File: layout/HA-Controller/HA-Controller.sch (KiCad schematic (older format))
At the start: 62 parts, among them J1 Conn_01x03, J2 Conn_01x06, J3 Conn_01x08, J4 Conn_01x10, J5 Conn_01x08, J6 Conn_01x15, J7 Conn_01x15, J8 Conn_01x04, J9 Conn_01x04, K1 FINDER-44.62, K2 FINDER-44.62, M1 Jumper, M2 Jumper, Q1 BC547, Q2 BC547, U1 ESP-12E, U2 IRM-15-24, U3 TSR_1-2450

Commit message: Layout abgespeckt
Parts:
- removed 180K: 1K2, Resistor_THT:R_Axial_DIN0309_L9.0mm_D3.2mm_P12.70mm_Horizontal, symbol Device:R
- removed C4, C6, C8: 100n, Capacitor_SMD:C_0603_1608Metric, symbol Device:C_Small
- removed C7: 10uF/50V, Capacitor_THT:CP_Radial_D6.3mm_P2.50mm, symbol Device:CP_Small
- removed D1: 1N4148, Diode_THT:D_DO-35_SOD27_P7.62mm_Horizontal, symbol Diode:1N4148
- removed D3, D6: LED_Small, LED_THT:LED_D3.0mm, symbol Device:LED_Small
- removed F1: 0,1A, Fuse:Fuseholder_Cylinder-5x20mm_Stelvio-Kontek_PTF78_Horizontal_Open, symbol Device:Fuse_Small
- removed J1: Conn_01x03, Connector_Phoenix_MSTB:PhoenixContact_MSTBA_2,5_3-G-5,08_1x03_P5.08mm_Horizontal, symbol Connector_Generic:Conn_01x03
- removed J3, J5: Conn_01x08, Connector_PinSocket_2.54mm:PinSocket_1x08_P2.54mm_Vertical, symbol Connector_Generic:Conn_01x08
- removed JP1: Jumper_NC_Small, Connector_PinHeader_2.54mm:PinHeader_1x02_P2.54mm_Vertical, symbol Device:Jumper_NC_Small
- removed K2: FINDER-44.62, Relay_THT:Relay_DPDT_Finder_40.52, symbol Relay:FINDER-44.62
- removed M1: Jumper, kp-Bom_only:Jumper, symbol kp-Bom_only:Jumper
- removed Q1: BC547, Package_TO_SOT_THT:TO-92_Inline, symbol Transistor_BJT:BC547
- removed R1: 4K7, Resistor_THT:R_Axial_DIN0309_L9.0mm_D3.2mm_P12.70mm_Horizontal, symbol Device:R
- removed R15, R9: 1K5, Resistor_THT:R_Axial_DIN0309_L9.0mm_D3.2mm_P12.70mm_Horizontal, symbol Device:R
- removed R2: 470, Resistor_THT:R_Axial_DIN0309_L9.0mm_D3.2mm_P12.70mm_Horizontal, symbol Device:R
- removed R5: dnf_470, Resistor_THT:R_Axial_DIN0309_L9.0mm_D3.2mm_P12.70mm_Horizontal, symbol Device:R
- removed R6: dnf_2K2, Resistor_THT:R_Axial_DIN0309_L9.0mm_D3.2mm_P12.70mm_Horizontal, symbol Device:R
- removed RV2: 24V, Varistor:RV_Disc_D7mm_W3.4mm_P5mm, symbol Device:Varistor
- removed U1: ESP-12E, RF_Module:ESP-12E, symbol RF_Module:ESP-12E
- removed U2: IRM-15-24, Zielke:NT-Meanwell-IRM-15, symbol Powersupply:Powersupply
- removed U3: TSR_1-2450, Converter_DCDC:Converter_DCDC_TRACO_TSR-1_THT, symbol Regulator_Switching:TSR_1-2450
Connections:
- net +24V is gone; now on net +5V: D2.1 (K), J4.5 (Pin_5), K1.A1, R10.1
- net K2-12 is gone; now on net +5V: J2.1 (Pin_1)
- net K2-14 is gone; now on net GND: J2.2 (Pin_2)
- net SWMaxNC is gone; now on net GPIO12: J4.4 (Pin_4), RV1.1
- net ADC: no longer names the net of J6.1 (Pin_1)
- net K2-11: no longer names the net of J2.3 (Pin_3)
- net Level: no longer names the net of J4.2 (Pin_2)
- net SWPumpOff renamed SW_Reserved
- no-connect marks 12 -> 11
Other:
- note added: "Door = close = 0V"
- note added: "GND"
- note added: "Open Door"
- note added: "S2\nclosed=\nReserved on\nopen =\nReserved off"
- note added: "SWDoor"
- note added: "SW_Reserved"
- note removed: "(0-1,054V)"
- note removed: "(10K)"
- note removed: "(2K2)"
- note removed: "(470)"
- note removed: "0-3.235V"
- note removed: "0-5V"
- note removed: "230V"
- note removed: "L1"
- note removed: "Max = close = 0V"
- note removed: "N"
- note removed: "Pump L1"
- note removed: "Pump N"
- note removed: "S1 (On/Off)"
- note removed: "S2 (Auto/Off)\nclosed=\nPump on\nopen =\nPump off"
- note removed: "S2\nclosed=\nPump on\nopen =\nPump off"
- note removed: "SWMaxNC"
- note removed: "SWPumpOff"

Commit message: Layout abgespeckt
Signed-off-by: Claus Zielke <info@cszielke.de>
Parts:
- removed J4: Conn_01x10, Connector_Phoenix_MSTB:PhoenixContact_MSTBA_2,5_10-G-5,08_1x10_P5.08mm_Horizontal, symbol Connector_Generic:Conn_01x10
- removed K1: FINDER-44.62, Relay_THT:Relay_DPDT_Finder_40.52, symbol Relay:FINDER-44.62
- removed R13: 1K, Resistor_THT:R_Axial_DIN0309_L9.0mm_D3.2mm_P12.70mm_Horizontal, symbol Device:R
- removed RV1, RV3, RV4: 24V, Varistor:RV_Disc_D7mm_W3.4mm_P5mm, symbol Device:Varistor
- added J4: Conn_01x06, Connector_Phoenix_MSTB:PhoenixContact_MSTBA_2,5_6-G-5,08_1x06_P5.08mm_Horizontal, symbol Connector_Generic:Conn_01x06
- added K1: G5V-2, Relay_THT:Relay_DPDT_Omron_G5V-2, symbol Relay:G5V-2
- R11: value 47K -> 3K3
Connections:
- net +5V: now also J4.4 (Pin_4), K1.1
- net GND: now also R12.2, J4.1 (Pin_1)
- net GPIO12: now also J4.2 (Pin_2)
- net K1-11: now also K1.13, K1.4
- net K1-12: now also K1.11, K1.6
- net K1-14: now also K1.8, K1.9
- net SW_Reserved: now also J4.3 (Pin_3)
- net at D2.2 (A), D4.1 (K), Q2.1 (C): now also K1.16
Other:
- note added: "2.9V"
- note removed: "0-29V"
- note removed: "0-3,13V"
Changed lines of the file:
@@
 $EndComp
 $Comp
-L Connector_Generic:Conn_01x10 J4
-U 1 1 5F26FC1D
-P 10050 3750
-F 0 "J4" H 10000 4350 50  0000 L CNN
-F 1 "Conn_01x10" H 10000 4250 50  0000 L CNN
-F 2 "Connector_Phoenix_MSTB:PhoenixContact_MSTBA_2,5_10-G-5,08_1x10_P5.08mm_Horizontal" H 10050 3750 50  0001 C CNN
-F 3 "~" H 10050 3750 50  0001 C CNN
-	1    10050 3750
-	1    0    0    -1
-$EndComp
-$Comp
 L Connector_Generic:Conn_01x06 J2
 U 1 1 5F272DC4
@@
 Wire Wire Line
 	9800 2650 9400 2650
-Wire Wire Line
-	9450 3950 9850 3950
-Wire Wire Line
-	9500 4250 9850 4250
-Text Label 9500 3350 0    50   ~ 0
+Text Label 9500 3550 0    50   ~ 0
 GND
 $Comp
 L power:GND #PWR02
 U 1 1 5F2781D4
-P 8350 3350
-F 0 "#PWR02" H 8350 3100 50  0001 C CNN
-F 1 "GND" H 8355 3177 50  0000 C CNN
-F 2 "" H 8350 3350 50  0001 C CNN
-F 3 "" H 8350 3350 50  0001 C CNN
-	1    8350 3350
-	0    1    1    0
+P 9400 3550
+F 0 "#PWR02" H 9400 3300 50  0001 C CNN
+F 1 "GND" H 9405 3377 50  0000 C CNN
+F 2 "" H 9400 3550 50  0001 C CNN
+F 3 "" H 9400 3550 50  0001 C CNN
+	1    9400 3550
+	-1   0    0    1
 $EndComp
-Wire Wire Line
-	8350 3350 8650 3350
 Text Label 9500 3650 0    50   ~ 0
 GPIO12
@@
 	7250 2150 7250 2100
 Connection ~ 7250 2150
-$Comp
-L Device:Varistor RV1
-U 1 1 5F3952B4
-P 8650 3150
-F 0 "RV1" H 8753 3196 50  0000 L CNN
-F 1 "24V" H 8753 3105 50  0000 L CNN
-F 2 "Varistor:RV_Disc_D7mm_W3.4mm_P5mm" V 8580 3150 50  0001 C CNN
-F 3 "~" H 8650 3150 50  0001 C CNN
-	1    8650 3150
-	1    0    0    -1
-$EndComp
 Wire Wire Line
 	7550 2300 7550 2250
@@
 Text Label 7650 3250 1    50   ~ 0
 K1-11
-$Comp
-L Device:Varistor RV3
-U 1 1 5F3C2F6A
-P 9350 3150
-F 0 "RV3" H 9453 3196 50  0000 L CNN
-F 1 "24V" H 9453 3105 50  0000 L CNN
-F 2 "Varistor:RV_Disc_D7mm_W3.4mm_P5mm" V 9280 3150 50  0001 C CNN
-F 3 "~" H 9350 3150 50  0001 C CNN
-	1    9350 3150
-	1    0    0    -1
-$EndComp
-Wire Wire Line
-	9350 3300 9350 3350
-Connection ~ 9350 3350
-Wire Wire Line
-	9350 3350 9850 3350
-Wire Wire Line
-	9350 3000 9450 3000
-Wire Wire Line
-	9450 3000 9450 3550
-Connection ~ 9450 3550
-Wire Wire Line
-	9450 3550 9850 3550
-Wire Wire Line
-	8350 3550 9450 3550
-Wire Wire Line
-	8650 3350 8650 3300
-Connection ~ 8650 3350
-Wire Wire Line
-	8650 3000 8750 3000
-Wire Wire Line
-	8750 3000 8750 3650
-Wire Wire Line
-	8750 3650 9850 3650
 Text Label 9400 2650 0    50   ~ 0
 K1-11
@@
 	1    0    0    -1
 $EndComp
-$Comp
-L power:+5V #PWR0107
-U 1 1 5F584395
-P 8350 3550
-F 0 "#PWR0107" H 8350 3400 50  0001 C CNN
-F 1 "+5V" V 8365 3678 50  0000 L CNN
-F 2 "" H 8350 3550 50  0001 C CNN
-F 3 "" H 8350 3550 50  0001 C CNN
-	1    8350 3550
-	0    -1   -1   0
-$EndComp
-Wire Wire Line
-	8750 3650 8300 3650
-Connection ~ 8750 3650
-Text Label 8300 3650 0    50   ~ 0
-GPIO12
-Text Label 9550 3550 0    50   ~ 0
-+5V
 NoConn ~ 4550 5800
 NoConn ~ 800  6350
@@
 NoConn ~ 800  5750
 NoConn ~ 800  5650
-Text Label 9450 4050 0    50   ~ 0
-GPIO4_DAT
-Text Label 9450 4150 0    50   ~ 0
-GPIO5_CLK
-Wire Wire Line
-	9450 4050 9850 4050
-Wire Wire Line
-	9450 4150 9850 4150
-$Comp
-L power:GND #PWR0108
-U 1 1 5F2E7337
-P 9500 4250
-F 0 "#PWR0108" H 9500 4000 50  0001 C CNN
-F 1 "GND" H 9505 4077 50  0000 C CNN
-F 2 "" H 9500 4250 50  0001 C CNN
-F 3 "" H 9500 4250 50  0001 C CNN
-	1    9500 4250
-	1    0    0    -1
-$EndComp
 Wire Wire Line
 	6000 4950 6400 4950
@@
 Text Label 6400 4950 2    50   ~ 0
 VI2C
-Text Label 9450 3950 0    50   ~ 0
-VI2C
 Wire Notes Line
 	10100 2550 11050 2550
@@
 Wire Wire Line
 	7250 3050 7250 3200
-$Comp
-L Relay:FINDER-44.62 K1
-U 1 1 5F40BA32
-P 7650 2600
-F 0 "K1" H 8280 2646 50  0000 L CNN
-F 1 "FINDER-44.62" H 7700 2200 50  0000 L CNN
-F 2 "Relay_THT:Relay_DPDT_Finder_40.52" H 9000 2570 50  0001 C CNN
-F 3 "http://gfinder.findernet.com/assets/Series/359/S44EN.pdf" H 7450 2600 50  0001 C CNN
-	1    7650 2600
-	1    0    0    -1
-$EndComp
 Wire Wire Line
 	8050 2900 8050 2950
@@
 Wire Wire Line
 	7750 2200 7750 1900
-Wire Wire Line
-	9850 3850 9250 3850
-Wire Wire Line
-	9250 3850 9250 4000
-Wire Wire Line
-	9250 4000 9150 4000
-Text Label 8750 4000 0    50   ~ 0
+Text Label 8750 3750 0    50   ~ 0
 SW_Reserved
 $Comp
 L power:GND #PWR01
 U 1 1 5F2EE7EB
-P 8750 5550
-F 0 "#PWR01" H 8750 5300 50  0001 C CNN
-F 1 "GND" H 8755 5377 50  0000 C CNN
-F 2 "" H 8750 5550 50  0001 C CNN
-F 3 "" H 8750 5550 50  0001 C CNN
-	1    8750 5550
+P 8750 5200
+F 0 "#PWR01" H 8750 4950 50  0001 C CNN
+F 1 "GND" H 8755 5027 50  0000 C CNN
+F 2 "" H 8750 5200 50  0001 C CNN
+F 3 "" H 8750 5200 50  0001 C CNN
+	1    8750 5200
 	1    0    0    -1
 $EndComp
@@
 Wire Wire Line
 	8350 4800 8750 4800
-Wire Wire Line
-	8750 5500 8750 5550
-Wire Wire Line
-	8750 4000 8750 4400
 Text Label 8350 4800 0    50   ~ 0
 GPIO13
 Text Notes 8800 4400 0    50   ~ 0
-0-29V
+5V
 Text Notes 8300 4900 0    50   ~ 0
-0-3,13V
+2.9V
 $Comp
 L Device:LED_Small D5
@@
 Wire Wire Line
 	2200 900  2200 950
-$Comp
-L Device:Varistor RV4
-U 1 1 5F4C36C4
-P 9150 4200
-F 0 "RV4" H 9253 4246 50  0000 L CNN
-F 1 "24V" H 9253 4155 50  0000 L CNN
-F 2 "Varistor:RV_Disc_D7mm_W3.4mm_P5mm" V 9080 4200 50  0001 C CNN
-F 3 "~" H 9150 4200 50  0001 C CNN
-	1    9150 4200
-	1    0    0    -1
-$EndComp
-Wire Wire Line
-	9150 4000 9150 4050
-Connection ~ 9150 4000
-Wire Wire Line
-	9150 4000 8750 4000
-$Comp
-L power:GND #PWR031
-U 1 1 5F4D443C
-P 9150 4350
-F 0 "#PWR031" H 9150 4100 50  0001 C CNN
-F 1 "GND" H 9155 4177 50  0000 C CNN
-F 2 "" H 9150 4350 50  0001 C CNN
-F 3 "" H 9150 4350 50  0001 C CNN
-	1    9150 4350
-	1    0    0    -1
-$EndComp
 Text Label 3950 6400 0    50   ~ 0
 GPIO13
@@
 	10150 3850 10300 3850
 Wire Notes Line
-	10150 3350 10500 3350
+	10150 3550 10500 3550
 Wire Notes Line
-	10500 3350 10500 3100
+	10500 3550 10500 3100
 Text Notes 10950 3550 1    50   ~ 0
 Level 0-5V
@@
 GPIO16
 $Comp
-L Device:R R13
-U 1 1 5F2EE7F6
-P 8750 5350
-F 0 "R13" H 8820 5396 50  0000 L CNN
-F 1 "1K" H 8820 5305 50  0000 L CNN
-F 2 "Resistor_THT:R_Axial_DIN0309_L9.0mm_D3.2mm_P12.70mm_Horizontal" V 8680 5350 50  0001 C CNN
-F 3 "~" H 8750 5350 50  0001 C CNN
-	1    8750 5350
-	1    0    0    -1
-$EndComp
-$Comp
 L Device:R R12
 U 1 1 5F2EE7E5
@@
 P 8750 4550
 F 0 "R11" H 8820 4596 50  0000 L CNN
-F 1 "47K" H 8820 4505 50  0000 L CNN
+F 1 "3K3" H 8820 4505 50  0000 L CNN
 F 2 "Resistor_THT:R_Axial_DIN0309_L9.0mm_D3.2mm_P12.70mm_Horizontal" V 8680 4550 50  0001 C CNN
 F 3 "~" H 8750 4550 50  0001 C CNN
@@
 L power:+5V #PWR0105
 U 1 1 609B8C6F
-P 9550 3750
-F 0 "#PWR0105" H 9550 3600 50  0001 C CNN
-F 1 "+5V" V 9565 3878 50  0000 L CNN
-F 2 "" H 9550 3750 50  0001 C CNN
-F 3 "" H 9550 3750 50  0001 C CNN
-	1    9550 3750
+P 9550 3850
+F 0 "#PWR0105" H 9550 3700 50  0001 C CNN
+F 1 "+5V" V 9565 3978 50  0000 L CNN
+F 2 "" H 9550 3850 50  0001 C CNN
+F 3 "" H 9550 3850 50  0001 C CNN
+	1    9550 3850
 	0    -1   -1   0
 $EndComp
 Wire Wire Line
-	9850 3750 9550 3750
+	9850 3850 9550 3850
+$Comp
+L Relay:G5V-2 K1
+U 1 1 608ECD9D
+P 7650 2600
+F 0 "K1" H 8280 2646 50  0000 L CNN
+F 1 "G5V-2" H 8280 2555 50  0000 L CNN
+F 2 "Relay_THT:Relay_DPDT_Omron_G5V-2" H 8300 2550 50  0001 L CNN
+F 3 "http://omronfs.omron.com/en_US/ecb/products/pdf/en-g5v_2.pdf" H 7450 2600 50  0001 C CNN
+	1    7650 2600
+	1    0    0    -1
+$EndComp
 Wire Wire Line
-	8650 3350 9350 3350
+	9500 3650 9850 3650
+Wire Wire Line
+	9400 3550 9850 3550
+Wire Wire Line
+	8750 3750 8750 4400
+Wire Wire Line
+	8750 3750 9850 3750
+$Comp
+L Connector_Generic:Conn_01x06 J4
+U 1 1 6093D5B8
+P 10050 3750
+F 0 "J4" H 10000 4150 50  0000 L CNN
+F 1 "Conn_01x06" H 10000 4050 50  0000 L CNN
+F 2 "Connector_Phoenix_MSTB:PhoenixContact_MSTBA_2,5_6-G-5,08_1x06_P5.08mm_Horizontal" H 10050 3750 50  0001 C CNN
+F 3 "~" H 10050 3750 50  0001 C CNN
+	1    10050 3750
+	1    0    0    -1
+$EndComp
 $EndSCHEMATC

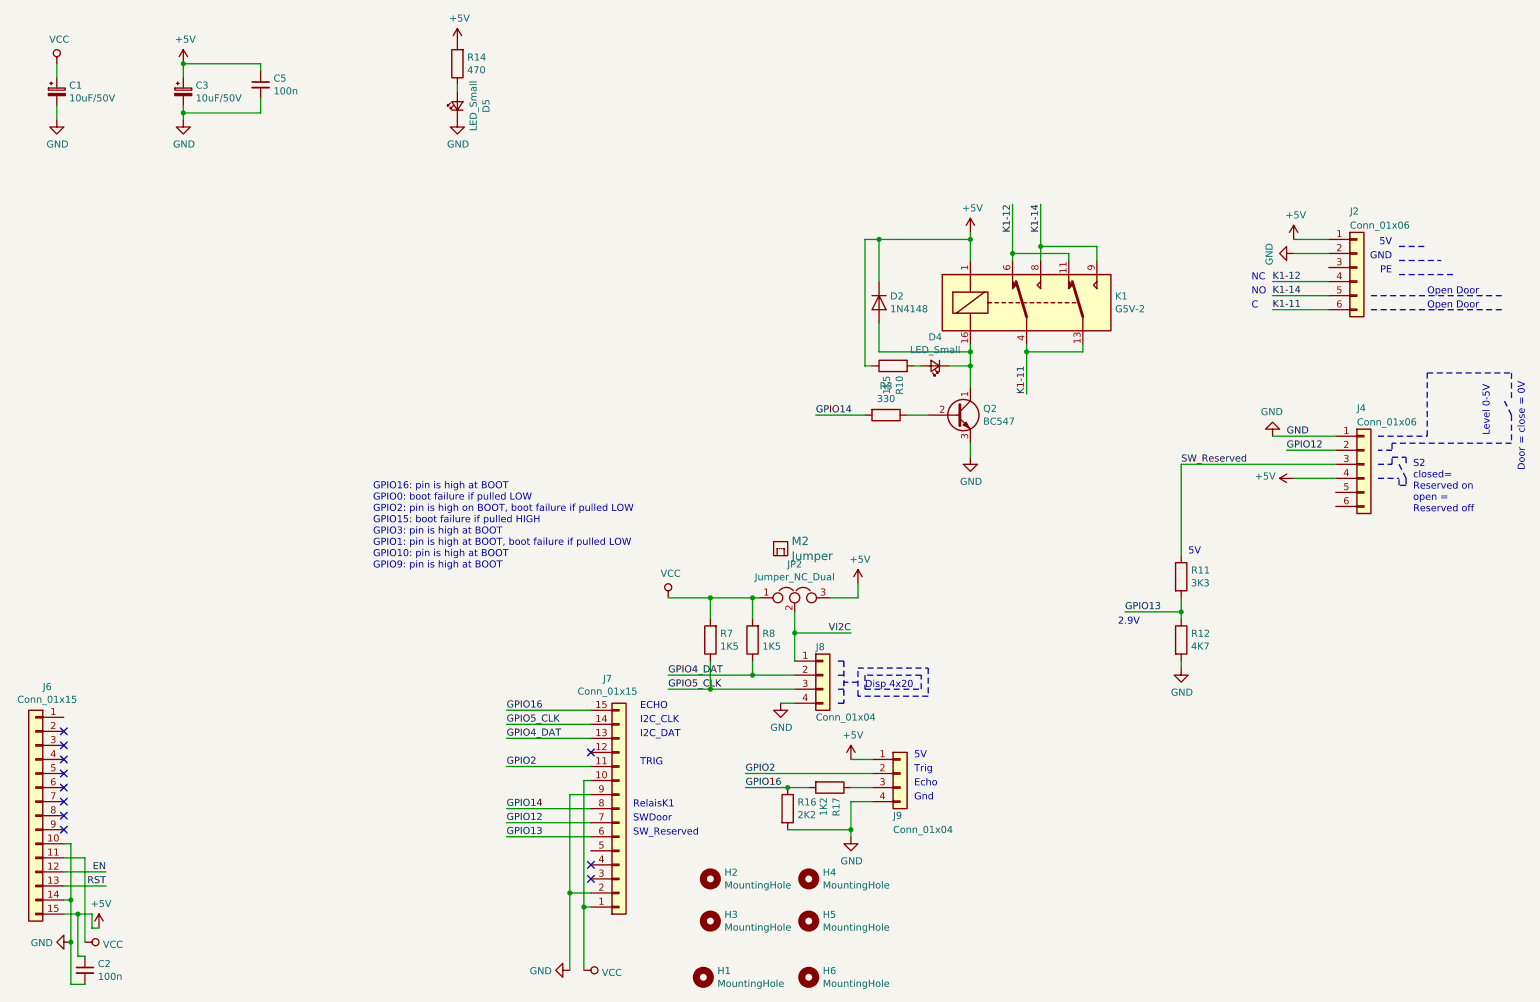
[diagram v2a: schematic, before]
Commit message: Layout für Verteilerdose und Lochraster optimiert
Signed-off-by: Claus Zielke <info@cszielke.de>
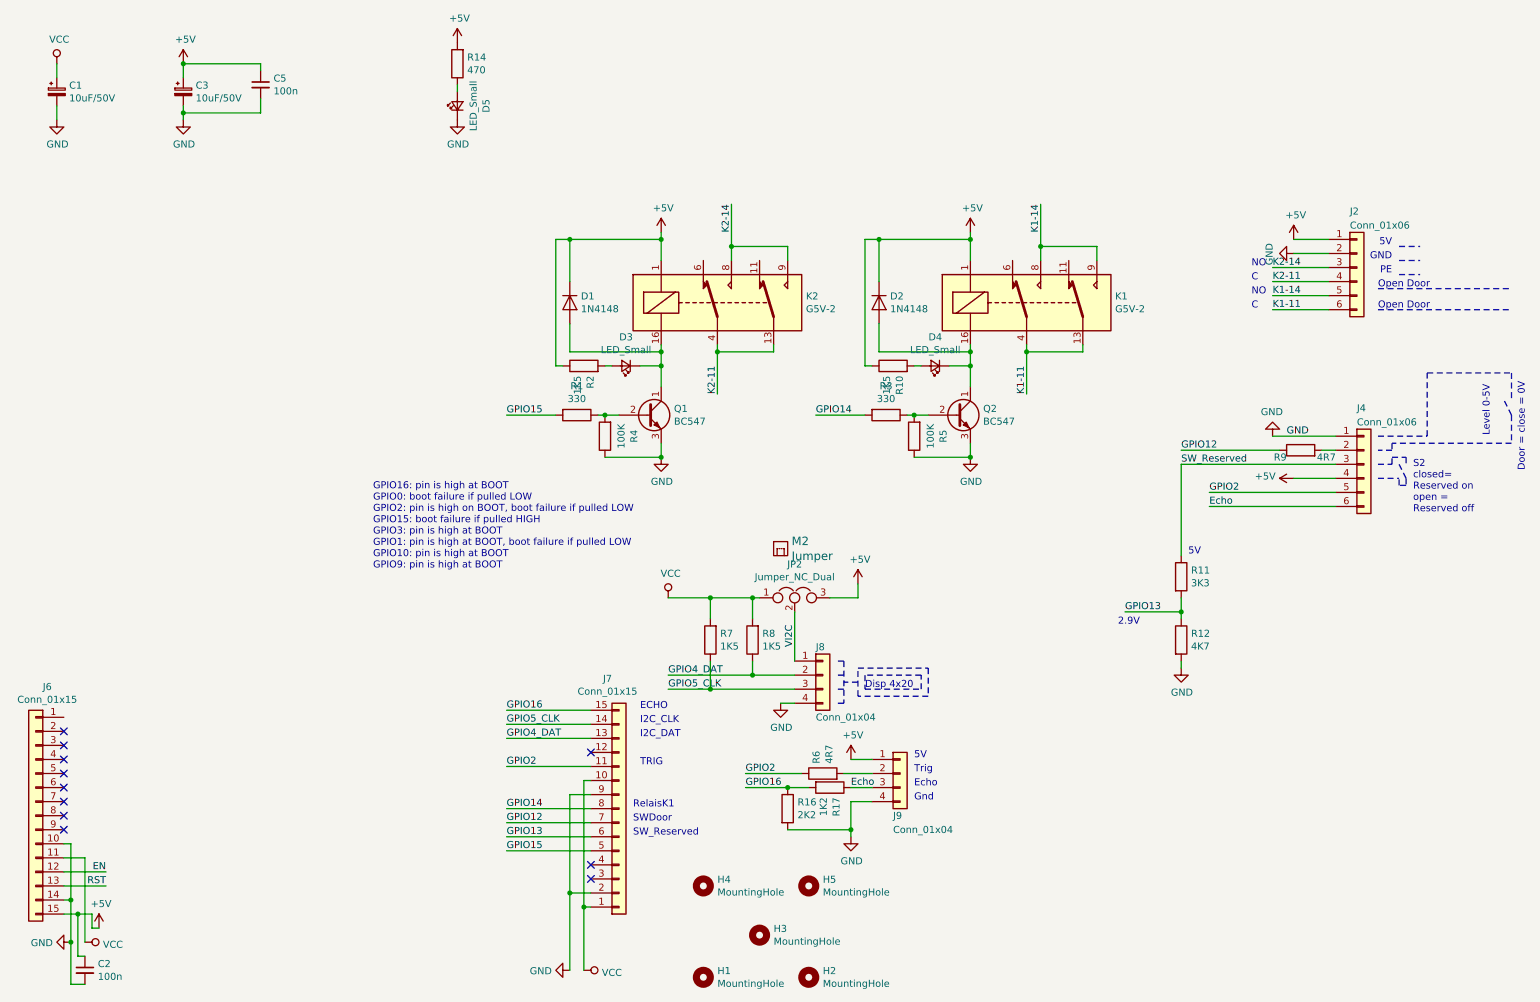
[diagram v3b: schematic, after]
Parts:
- removed H6: MountingHole, MountingHole:MountingHole_4.3mm_M4_ISO14580, symbol Mechanical:MountingHole
- added D1: 1N4148, Diode_THT:D_DO-35_SOD27_P7.62mm_Horizontal, symbol Diode:1N4148
- added D3: LED_Small, LED_THT:LED_D3.0mm, symbol Device:LED_Small
- added K2: G5V-2, Relay_THT:Relay_DPDT_Omron_G5V-2, symbol Relay:G5V-2
- added Q1: BC547, Package_TO_SOT_THT:TO-92_Inline, symbol Transistor_BJT:BC547
- added R1: 330, Resistor_SMD:R_0603_1608Metric, symbol Device:R
- added R2: 1K5, Resistor_SMD:R_0603_1608Metric, symbol Device:R
- added R4, R5: 100K, Resistor_SMD:R_0603_1608Metric, symbol Device:R
- added R6, R9: 4R7, Resistor_SMD:R_0603_1608Metric, symbol Device:R
- R10, R11, R12, R14, R16, R17, R3, R7, R8: footprint Resistor_THT:R_Axial_DIN0309_L9.0mm_D3.2mm_P12.70mm_Horizontal -> Resistor_SMD:R_0603_1608Metric
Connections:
- net +5V: now also D1.1 (K), K2.1, R2.1
- net GND: now also Q1.3 (E), R4.1, R5.1
- net GPIO12: now also R9.1; no longer J4.2 (Pin_2)
- net GPIO2: now also J4.5 (Pin_5), R6.1; no longer J9.2 (Pin_2)
- net K2-14: now reaches J2.3 (Pin_3)
- net K2-14: now also K2.8, K2.9
- net GPIO15: now reaches J7.5 (Pin_5)
- net GPIO15: now also R1.2
- net at Q2.2 (B), R3.1: now also R5.2
- net Echo: now reaches J9.3 (Pin_3), R17.1
- net Echo: now also J4.6 (Pin_6)
- removed net K1-12: J2.4 (Pin_4), K1.11, K1.6
- new net: J9.2 (Pin_2), R6.2
- new net: J4.2 (Pin_2), R9.2
- new net: D1.2 (A), D3.1 (K), K2.16, Q1.1 (C)
- new net: Q1.2 (B), R1.1, R4.2
- new net: D3.2 (A), R2.2
- new net K2-11: J2.4 (Pin_4), K2.13, K2.4
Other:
- note removed: "NC"
- moved on the sheet: H2, H3, H4, H5
